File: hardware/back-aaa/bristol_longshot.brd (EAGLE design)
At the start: 14 x 64 mm, 7 parts, among them U4 ADP1607ACPZN-R7

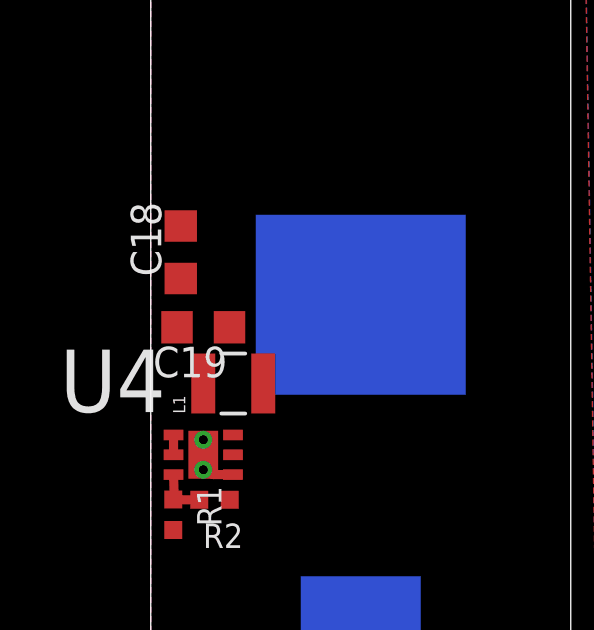
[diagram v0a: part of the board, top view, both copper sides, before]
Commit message: Added partslist, updated parts for back-aaa
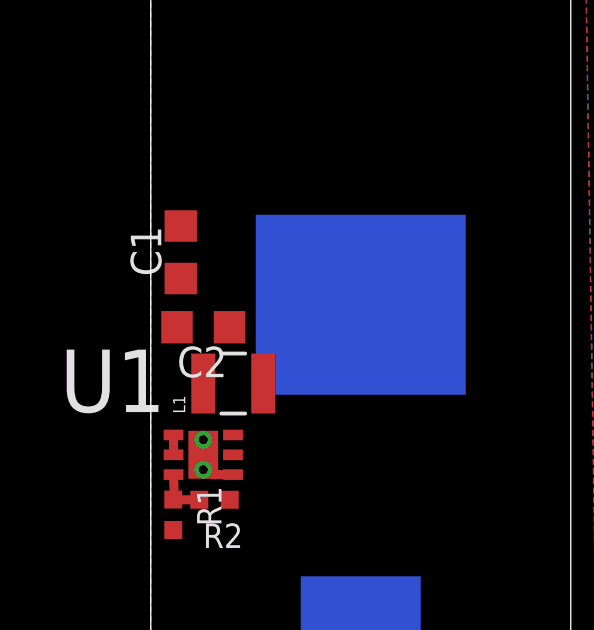
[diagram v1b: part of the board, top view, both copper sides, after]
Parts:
- renumbered C18 to C1, C19 to C2, U4 to U1
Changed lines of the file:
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@@
 <element name="L1" library="SparkFun" package="1007" value="2.2µH" x="2.75" y="17.875" rot="R90"/>
 <element name="U$2" library="fbri" package="AA" value="AA_HOLDER" x="7" y="32" rot="MR0"/>
-<element name="C19" library="resistor" package="C0603K" value="10µF" x="1.75" y="19.75" rot="R180"/>
-<element name="U4" library="ADP1607" package="DFN200X200X60-7N" value="ADP1607ACPZN-R7" x="1.75" y="15.5">
+<element name="C2" library="resistor" package="C0603K" value="10µF" x="1.75" y="19.75" rot="R180"/>
+<element name="U1" library="ADP1607" package="DFN200X200X60-7N" value="ADP1607ACPZN-R7" x="1.75" y="15.5">
 <attribute name="PACKAGE" value="6LFCSP" x="1.75" y="15.5" size="1.778" layer="27" display="off"/>
 <attribute name="OC_NEWARK" value="54W6610" x="1.75" y="15.5" size="1.778" layer="27" display="off"/>
@@
 <element name="R1" library="microbuilder_v3" package="_0402" value="100kΩ" x="0.75" y="13.5" rot="R270"/>
 <element name="R2" library="microbuilder_v3" package="_0402" value="240kΩ" x="2.125" y="14" rot="R180"/>
-<element name="C18" library="resistor" package="C0603K" value="10µF" x="1" y="22.25" rot="R90"/>
+<element name="C1" library="resistor" package="C0603K" value="10µF" x="1" y="22.25" rot="R90"/>
 </elements>
 <signals>
@@
 <contactref element="U$2" pad="-2"/>
 <contactref element="U$2" pad="-1"/>
-<contactref element="C19" pad="2"/>
-<contactref element="U4" pad="4"/>
-<contactref element="U4" pad="7"/>
+<contactref element="C2" pad="2"/>
+<contactref element="U1" pad="4"/>
+<contactref element="U1" pad="7"/>
 <contactref element="R2" pad="1"/>
-<contactref element="C18" pad="2"/>
+<contactref element="C1" pad="2"/>
 <via x="1.75" y="16" extent="1-16" drill="0.3"/>
 <via x="1.75" y="15" extent="1-16" drill="0.3"/>
@@
 </signal>
 <signal name="1.8V">
-<contactref element="C19" pad="1"/>
-<contactref element="U4" pad="6"/>
+<contactref element="C2" pad="1"/>
+<contactref element="U1" pad="6"/>
 <contactref element="R1" pad="2"/>
 <wire x1="2.7406" y1="16.1604" x2="2.625" y2="19.75" width="0" layer="19" extent="1-1"/>
@@
 <signal name="1.2V">
 <contactref element="U$2" pad="+2"/>
-<contactref element="U4" pad="1"/>
-<contactref element="U4" pad="2"/>
+<contactref element="U1" pad="1"/>
+<contactref element="U1" pad="2"/>
 <contactref element="L1" pad="1"/>
-<contactref element="C18" pad="1"/>
+<contactref element="C1" pad="1"/>
 <wire x1="0.7594" y1="15.5" x2="0.7594" y2="16.1604" width="0.3048" layer="1"/>
 <wire x1="1" y1="21.375" x2="7" y2="43.5" width="0" layer="19" extent="1-16"/>
@@
 </signal>
 <signal name="SW">
-<contactref element="U4" pad="5"/>
+<contactref element="U1" pad="5"/>
 <contactref element="L1" pad="2"/>
 <wire x1="2.7406" y1="15.5" x2="3.75" y2="17.875" width="0" layer="19" extent="1-1"/>
 </signal>
 <signal name="FB">
-<contactref element="U4" pad="3"/>
+<contactref element="U1" pad="3"/>
 <contactref element="R2" pad="2"/>
 <contactref element="R1" pad="1"/>

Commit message: aaa-board mostly done
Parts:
- added C3: 100pF, microbuilder_v3:_0402
- added U$12: M04X2, fbri:M04X2
- moved L1 41.8 mm to (11.5, 58.8)
- moved R1 41.7 mm to (12.5, 53.5), turned to 0 degrees
- moved U1 40.9 mm to (11.5, 55.2)
- moved C2 40.9 mm to (7.50, 60.2)
- moved R2 40.1 mm to (12.5, 52.8)
- moved C1 37.1 mm to (7.50, 58.8), turned to 180 degrees
- flipped U$2 to the top
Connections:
- removed net +2: U$2.+1
- new net +: U$2.+2
- net 1.2V: now also U$12.P$5, U$2.+1; no longer U$2.+2
- net 1.8V: now also C3.1, U$12.P$3
- net GND: now also C3.2, U$12.P$1, U$12.P$2, U$12.P$4, U$12.P$6
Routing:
- net 1.8V: track 0.00 -> 18.9 mm, vias 0 -> 2
- net 1.2V: track 0.66 -> 15.5 mm, vias 0 -> 1
- net SW: track 0.00 -> 4.36 mm
- net FB: track 1.72 -> 2.75 mm
- net GND: track 1.46 -> 1.06 mm, vias 2 -> 40
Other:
- board text added: "AAA Battery"
- board text removed: "v0.96.0"

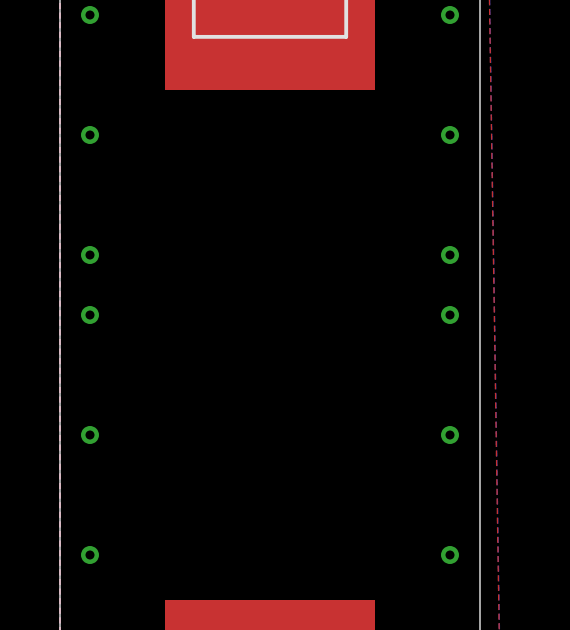
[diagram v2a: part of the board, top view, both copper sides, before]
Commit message: Added cream to battery contacts on aaa-board
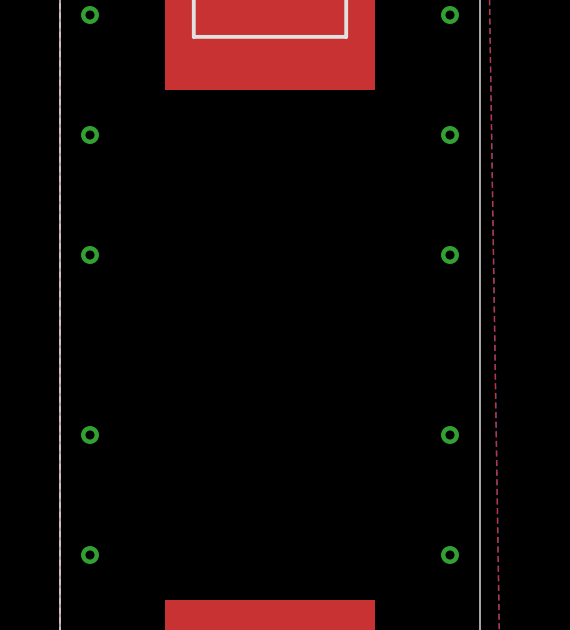
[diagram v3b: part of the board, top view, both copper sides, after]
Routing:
- net GND: vias 40 -> 38
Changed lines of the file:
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@@
 <via x="1" y="39" extent="1-16" drill="0.3"/>
 <via x="1" y="35" extent="1-16" drill="0.3"/>
-<via x="1" y="33" extent="1-16" drill="0.3"/>
 <via x="13" y="5" extent="1-16" drill="0.3"/>
 <via x="13" y="9" extent="1-16" drill="0.3"/>
@@
 <via x="13" y="25" extent="1-16" drill="0.3"/>
 <via x="13" y="29" extent="1-16" drill="0.3"/>
-<via x="13" y="33" extent="1-16" drill="0.3"/>
 <via x="13" y="35" extent="1-16" drill="0.3"/>
 <via x="13" y="39" extent="1-16" drill="0.3"/>
